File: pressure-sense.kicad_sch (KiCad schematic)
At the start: 6 parts, among them U2 BMP581, U3 BMP581

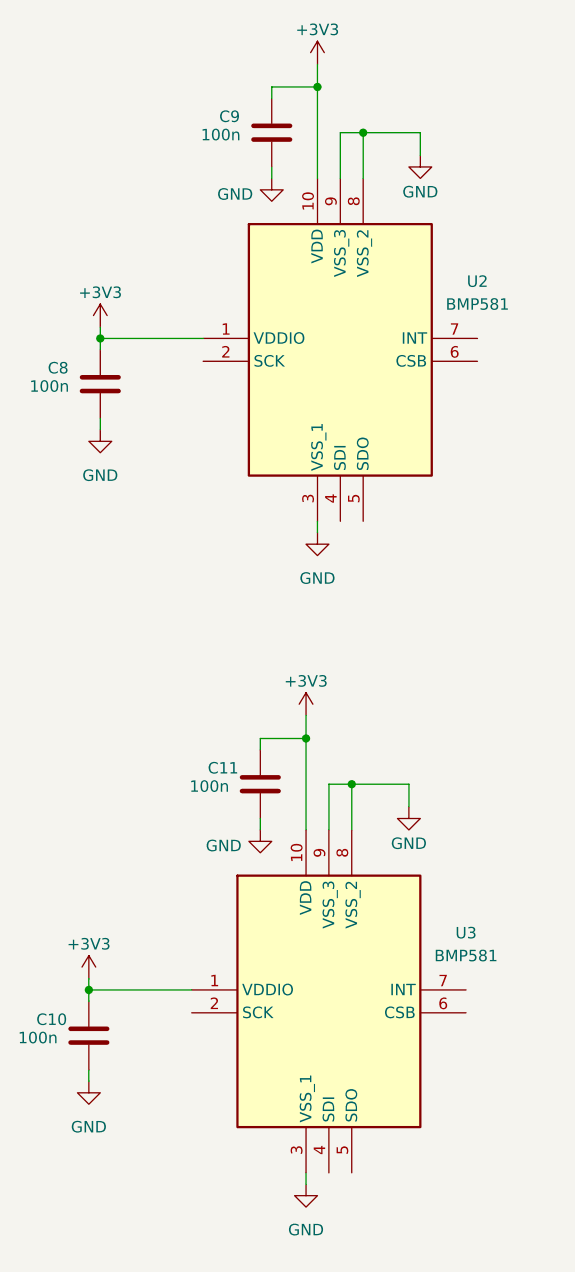
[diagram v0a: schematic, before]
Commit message: fix: bmp581 config
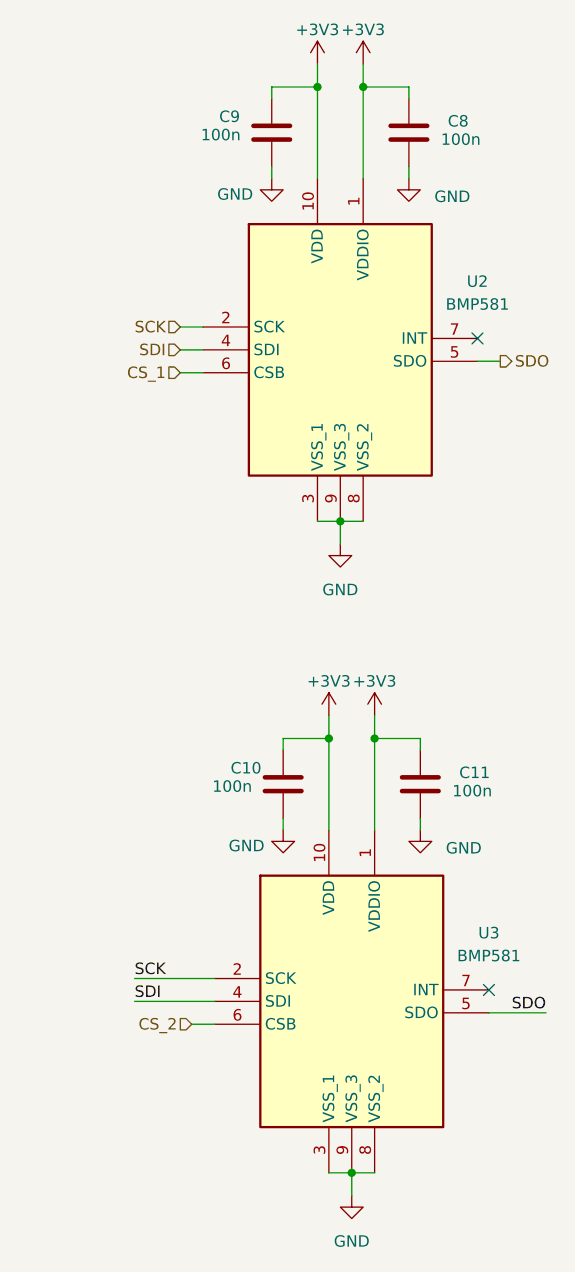
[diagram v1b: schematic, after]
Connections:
- net SCK: now reaches U3.2 (SCK)
- net SCK: now also U2.2 (SCK)
- net SDI: now reaches U3.4 (SDI)
- net SDI: now also U2.4 (SDI)
- net SDO: now reaches U3.5 (SDO)
- net SDO: now also U2.5 (SDO)
- net CS_2: now reaches U3.6 (CSB)
- net CS_1: now reaches U2.6 (CSB)
- no-connect marks 0 -> 2
